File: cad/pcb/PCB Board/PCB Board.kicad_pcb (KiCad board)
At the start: 2 copper layers, 14 parts, among them J1 Conn_01x02_Pin, J2 Conn_01x03_Pin, J3 Conn_01x04_Pin, J4 Conn_01x03_Pin, Q1 BC547, Q2 BC547, Q3 BC547, SW1 SW_Push, SW2 SW_Push, SW3 SW_Push, SW4 SW_Push

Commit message: started work on the pcb and cad data
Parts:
- removed J4: Conn_01x03_Pin, Connector_JST:JST_XH_B3B-XH-A_1x03_P2.50mm_Vertical
- removed Q1, Q2, Q3: BC547, Package_TO_SOT_THT:TO-92_Inline
- removed R1, R2, R3: R33K, Resistor_THT:R_Axial_DIN0204_L3.6mm_D1.6mm_P7.62mm_Horizontal
- added StepUp1: ~, Library:StepUp, B.Cu at (143.2, 64.5)
- added U1: BOB-12009, BOB-12009:CONV_BOB-12009, B.Cu at (142.9, 88.1)
- added U2: ~, Library:Lolin32 Lite, B.Cu at (135.5, 50.4)
- J1: value Conn_01x02_Pin -> POWER; moved to B.Cu
- J2: value Conn_01x03_Pin -> LED+
- J3: value Conn_01x04_Pin -> Conn_01x02_Pin; footprint Connector_JST:JST_XH_B4B-XH-A_1x04_P2.50mm_Vertical -> Connector_Wire:SolderWire-0.1sqmm_1x02_P3.6mm_D0.4mm_OD1mm; moved to B.Cu
- moved SW4 118.7 mm to (93.0, 78.2), turned to 90 degrees
- moved J1 80.2 mm to (101.0, 63.0), turned to 180 degrees
- moved SW3 77.4 mm to (128.0, 107.2), turned to 180 degrees
- moved J2 73.8 mm to (124.2, 75.0), turned to 90 degrees
- moved J3 65.1 mm to (104.0, 70.2)
- moved SW2 62.7 mm to (158.0, 71.5), turned to -90 degrees
- moved SW1 62.5 mm to (122.0, 42.5)
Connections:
- J1 pad 2: Net-(J1-Pin_2) -> GND
- J2 pad 1: Net-(J1-Pin_1) -> Net-(J2-Pin_1)
- J2 pad 2: Net-(J1-Pin_1) -> Net-(J2-Pin_2)
- J2 pad 3: Net-(J1-Pin_1) -> Net-(J2-Pin_3)
- J3 pad 1: Net-(J3-Pin_1) -> Net-(J1-Pin_1)
- J3 pad 2: Net-(J3-Pin_2) -> GND
- SW1 pad 1: Net-(J3-Pin_4) -> Net-(J1-Pin_2)
- SW1 pad 2: Net-(J1-Pin_2) -> Net-(SW1-Pad2)
- SW2 pad 1: Net-(J3-Pin_4) -> GND
- SW2 pad 2: Net-(J1-Pin_2) -> Net-(SW1-Pad2)
- SW3 pad 1: Net-(J3-Pin_4) -> GND
- SW3 pad 2: Net-(J1-Pin_2) -> Net-(SW1-Pad2)
- SW4 pad 1: Net-(J3-Pin_4) -> GND
- SW4 pad 2: Net-(J1-Pin_2) -> Net-(SW1-Pad2)
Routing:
- net GND: track 0.00 -> 200.4 mm
- net Net-(SW1-Pad2): track 0.00 -> 141.0 mm
- net Net-(J1-Pin_1): track 0.00 -> 62.1 mm
- net Net-(U1-PadLV): track 0.00 -> 37.1 mm
- net Net-(J2-Pin_3): track 0.00 -> 31.1 mm
- net Net-(J2-Pin_2): track 0.00 -> 25.5 mm
- net Net-(J2-Pin_1): track 0.00 -> 16.4 mm
- net Net-(U1-PadLV1): track 0.00 -> 16.1 mm
- added copper zone on B.Cu, net GND
- added copper zone on F.Cu, net GND
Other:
- board outline added: 70 x 70 mm

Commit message: continued work on pcb
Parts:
- moved SW2 1.00 mm to (157.0, 71.5)
- moved SW1 0.75 mm to (122.0, 43.2)
- moved SW4 0.75 mm to (93.8, 78.2)
- moved SW3 0.50 mm to (128.0, 106.8)
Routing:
- net Net-(SW1-Pad2): track 141.0 -> 167.0 mm
- net GND: track 200.4 -> 199.4 mm
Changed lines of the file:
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@@
 	(footprint "Button_Switch_THT:SW_PUSH_6mm_H5mm"
 		(layer "F.Cu")
-		(at 122 42.5)
+		(at 122 43.25)
 		(descr "tactile push button, 6x6mm e.g. PHAP33xx series, height=5mm")
 		(tags "tact sw push 6mm")
 		(property "Reference" "SW1"
-			(at 3.25 -2 0)
+			(at 3.25 2.25 0)
 			(layer "F.SilkS")
 			(effects
@@
 	(footprint "Button_Switch_THT:SW_PUSH_6mm_H5mm"
 		(layer "F.Cu")
-		(at 158 71.5 -90)
+		(at 157 71.5 -90)
 		(descr "tactile push button, 6x6mm e.g. PHAP33xx series, height=5mm")
 		(tags "tact sw push 6mm")
 		(property "Reference" "SW2"
-			(at 3 -3.25 90)
+			(at 3.25 2 90)
 			(layer "F.SilkS")
 			(effects
@@
 		)
 		(fp_text user "${REFERENCE}"
-			(at -8.75 1.5 90)
+			(at -3.25 2.25 90)
 			(layer "F.Fab")
 			(effects
@@
 	(footprint "Button_Switch_THT:SW_PUSH_6mm_H5mm"
 		(layer "F.Cu")
-		(at 93 78.25 90)
+		(at 93.75 78.25 90)
 		(descr "tactile push button, 6x6mm e.g. PHAP33xx series, height=5mm")
 		(tags "tact sw push 6mm")
 		(property "Reference" "SW4"
-			(at 3.25 -2 -90)
+			(at -3.25 1.5 -90)
 			(layer "F.SilkS")
 			(effects
@@
 	(footprint "Button_Switch_THT:SW_PUSH_6mm_H5mm"
 		(layer "F.Cu")
-		(at 128 107.25 180)
+		(at 128 106.75 180)
 		(descr "tactile push button, 6x6mm e.g. PHAP33xx series, height=5mm")
 		(tags "tact sw push 6mm")
 		(property "Reference" "SW3"
-			(at 3.25 -2 180)
+			(at -3.75 0.25 180)
 			(layer "F.SilkS")
 			(effects
@@
 		(layer "Edge.Cuts")
 	)
+	(gr_circle
+		(center 125.5 75)
+		(end 159.5 75)
+		(stroke
+			(width 0.1)
+			(type default)
+		)
+		(fill none)
+		(layer "Margin")
+	)
 	(segment
 		(start 124.25 75)
@@
 	)
 	(segment
+		(start 128.5 47.75)
+		(end 122 47.75)
+		(width 0.2)
+		(layer "F.Cu")
+		(net 3)
+	)
+	(segment
+		(start 128 102.25)
+		(end 121.5 102.25)
+		(width 0.2)
+		(layer "F.Cu")
+		(net 3)
+	)
+	(segment
+		(start 152.5 78)
+		(end 152.5 71.5)
+		(width 0.2)
+		(layer "F.Cu")
+		(net 3)
+	)
+	(segment
+		(start 98.25 78.25)
+		(end 98.25 71.75)
+		(width 0.2)
+		(layer "F.Cu")
+		(net 3)
+	)
+	(segment
 		(start 139.257369 57.257369)
 		(end 117.742631 57.257369)
@@
 	)
 	(segment
-		(start 151.25 96.25)
-		(end 148.5 99)
+		(start 151.17 86.83)
+		(end 151.25 86.75)
 		(width 0.2)
 		(layer "F.Cu")
@@
 	)
 	(segment
-		(start 134.25 98.5)
-		(end 134.25 92.53)
+		(start 148 86.83)
+		(end 151.17 86.83)
 		(width 0.2)
 		(layer "F.Cu")
@@
 	)
 	(segment
-		(start 151.17 86.83)
-		(end 151.25 86.75)
+		(start 151.25 86.75)
+		(end 151.25 95.5)
 		(width 0.2)
 		(layer "F.Cu")
@@
 	)
 	(segment
-		(start 148 86.83)
-		(end 151.17 86.83)
+		(start 151.25 95.5)
+		(end 147.75 99)
 		(width 0.2)
 		(layer "F.Cu")
@@
 	)
 	(segment
-		(start 151.25 86.75)
-		(end 151.25 96.25)
+		(start 134.75 99)
+		(end 134.25 98.5)
 		(width 0.2)
 		(layer "F.Cu")
@@
 	)
 	(segment
-		(start 134.75 99)
-		(end 134.25 98.5)
+		(start 147.75 99)
+		(end 134.75 99)
 		(width 0.2)
 		(layer "F.Cu")
@@
 	)
 	(segment
-		(start 148.5 99)
-		(end 134.75 99)
+		(start 134.25 98.5)
+		(end 134.25 92.53)
 		(width 0.2)
 		(layer "F.Cu")
@@
 	)
 	(segment
-		(start 118 106.5)
-		(end 118.75 107.25)
+		(start 106.39 63.36)
+		(end 101.25 68.5)
 		(width 0.2)
 		(layer "B.Cu")
@@
 	)
 	(segment
-		(start 106.39 63.36)
-		(end 101.25 68.5)
+		(start 143.25 92)
+		(end 128 107.25)
 		(width 0.2)
 		(layer "B.Cu")
@@
 	)
 	(segment
-		(start 93 78.25)
-		(end 93 81.53886)
+		(start 158 78)
+		(end 158 71.5)
 		(width 0.2)
 		(layer "B.Cu")
@@
 	)
 	(segment
-		(start 143.25 92)
-		(end 128 107.25)
+		(start 93 71.75)
+		(end 93 81.53886)
 		(width 0.2)
 		(layer "B.Cu")
@@
 	)
 	(segment
-		(start 158 78)
-		(end 158 71.5)
+		(start 98.25 69.25)
+		(end 95.5 69.25)
 		(width 0.2)
 		(layer "B.Cu")
@@
 	)
 	(segment
-		(start 98.5 70.45)
-		(end 94.3 70.45)
+		(start 101.25 68.5)
+		(end 100.25 69.5)
 		(width 0.2)
 		(layer "B.Cu")
@@
 	)
 	(segment
-		(start 94.3 70.45)
-		(end 93 71.75)
+		(start 104 73.75)
+		(end 104 73.25)
 		(width 0.2)
 		(layer "B.Cu")
@@
 	)
 	(segment
-		(start 158 79.37)
-		(end 148 89.37)
+		(start 118 106.5)
+		(end 118.75 107.25)
 		(width 0.2)
 		(layer "B.Cu")
@@
 	)
 	(segment
-		(start 99.25 70.45)
-		(end 98.5 70.45)
+		(start 158 79.37)
+		(end 148 89.37)
 		(width 0.2)
 		(layer "B.Cu")
@@
 	)
 	(segment
-		(start 118.75 107.25)
-		(end 121.5 107.25)
+		(start 98.5 69.25)
+		(end 98.5 63)
 		(width 0.2)
 		(layer "B.Cu")
@@
 	)
 	(segment
-		(start 104 73.75)
-		(end 102.55 73.75)
+		(start 118.75 107.25)
+		(end 128 107.25)
 		(width 0.2)
 		(layer "B.Cu")
@@
 	)
 	(segment
-		(start 93 81.53886)
-		(end 117.96114 106.5)
+		(start 143.25 89.37)
+		(end 143.25 92)
 		(width 0.2)
 		(layer "B.Cu")
@@
 	)
 	(segment
-		(start 102.55 73.75)
-		(end 99.25 70.45)
+		(start 143.25 55)
+		(end 158 69.75)
 		(width 0.2)
 		(layer "B.Cu")
@@
 	)
 	(segment
-		(start 117.96114 106.5)
-		(end 118 106.5)
+		(start 95.5 69.25)
+		(end 93 71.75)
 		(width 0.2)
 		(layer "B.Cu")
@@
 	)
 	(segment
-		(start 143.25 89.37)
-		(end 143.25 92)
+		(start 100.25 69.5)
+		(end 98.5 69.5)
 		(width 0.2)
 		(layer "B.Cu")
@@
 	)
 	(segment
-		(start 143.25 55)
-		(end 158 69.75)
+		(start 106.39 62)
+		(end 106.39 63.36)
 		(width 0.2)
 		(layer "B.Cu")
@@
 	)
 	(segment
-		(start 106.39 62)
-		(end 106.39 63.36)
+		(start 93 81.53886)
+		(end 117.96114 106.5)
 		(width 0.2)
 		(layer "B.Cu")
@@
 	)
 	(segment
-		(start 93 71.75)
-		(end 93 78.25)
+		(start 117.96114 106.5)
+		(end 118 106.5)
 		(width 0.2)
 		(layer "B.Cu")
@@
 	)
 	(segment
-		(start 128 107.25)
-		(end 121.5 107.25)
+		(start 104 73.25)
+		(end 100.25 69.5)
 		(width 0.2)
 		(layer "B.Cu")
@@
 	)
 	(segment
-		(start 98.5 63)
-		(end 98.5 70.45)
+		(start 98.5 69.25)
+		(end 98.25 69.25)
 		(width 0.2)
 		(layer "B.Cu")
@@
 	)
 	(segment
-		(start 128 107.25)
-		(end 129.75 105.5)
+		(start 98.5 69.5)
+		(end 98.25 69.25)
 		(width 0.2)
 		(layer "B.Cu")
@@
 	)
 	(segment
-		(start 99.3 70.45)
-		(end 99.25 70.45)
+		(start 128 107.25)
+		(end 129.75 105.5)
 		(width 0.2)
 		(layer "B.Cu")
@@
 	)
 	(segment
-		(start 101.25 68.5)
-		(end 99.3 70.45)
+		(start 99.3 70.45)
+		(end 99.25 70.45)
 		(width 0.2)
 		(layer "B.Cu")

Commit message: updated pcbs
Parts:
- added J4: ON_OFF_SWITCH, Connector_Wire:SolderWire-0.5sqmm_1x02_P4.6mm_D0.9mm_OD2.1mm_Relief, B.Cu at (81.2, 48.8)
- added REF**: MountingHole_3.2mm_M3_Pad, MountingHole:MountingHole_3.2mm_M3_Pad, F.Cu at (101.8, 63.9)
- added REF**: MountingHole_3.2mm_M3_Pad, MountingHole:MountingHole_3.2mm_M3_Pad, F.Cu at (64.6, 101.1)
- added REF**: MountingHole_5.3mm_M5_DIN965, MountingHole:MountingHole_5.3mm_M5_DIN965, F.Cu at (80.5, 94.0)
- added REF**: MountingHole_3.2mm_M3_Pad, MountingHole:MountingHole_3.2mm_M3_Pad, F.Cu at (27.4, 63.9)
- added REF**: MountingHole_3.2mm_M3_Pad, MountingHole:MountingHole_3.2mm_M3_Pad, F.Cu at (64.6, 26.7)
- J1, StepUp1, U2: moved to F.Cu
- J3: value Conn_01x02_Pin -> BATTERY_CONNECTOR; footprint Connector_Wire:SolderWire-0.1sqmm_1x02_P3.6mm_D0.4mm_OD1mm -> Connector_Wire:SolderWire-0.5sqmm_1x02_P4.6mm_D0.9mm_OD2.1mm_Relief; moved to F.Cu
- SW1, SW2, SW3, SW4: moved to B.Cu
- U1: value BOB-12009 -> Lvl-Shifter; moved to F.Cu
- moved SW2 124.4 mm to (33.1, 60.4)
- moved U2 106.5 mm to (29.1, 46.8), turned to 45 degrees
- moved StepUp1 96.8 mm to (47.5, 78.6), turned to -45 degrees
- moved SW3 67.4 mm to (61.6, 95.4), turned to 0 degrees
- moved U1 62.2 mm to (82.0, 75.3), turned to -45 degrees
- moved SW1 55.5 mm to (67.6, 32.4), turned to 180 degrees
- moved J2 54.5 mm to (70.4, 82.9), turned to -45 degrees
- moved J3 34.6 mm to (76.7, 48.8), turned to 180 degrees
- moved J1 20.2 mm to (82.4, 55.2), turned to 0 degrees
- moved SW4 11.6 mm to (96.1, 66.9)
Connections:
- J1 pad 2: GND -> Net-(J1-Pin_2)
- J3 pad 1: Net-(J1-Pin_1) -> Net-(J3-Pin_1)
- J3 pad 2: GND -> Net-(J1-Pin_2)
- SW2 pad 1: GND -> Net-(J1-Pin_2)
- SW3 pad 1: GND -> Net-(J1-Pin_2)
- SW4 pad 1: GND -> Net-(J1-Pin_2)
- StepUp1 pad 1: GND -> Net-(J1-Pin_2)
- StepUp1 pad 2: Net-(J1-Pin_1) -> Net-(J3-Pin_1)
- U1 pad GND_1: GND -> Net-(J1-Pin_2)
- U1 pad GND_2: GND -> Net-(J1-Pin_2)
- U2 pad GND: GND -> Net-(J1-Pin_2)
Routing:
- net Net-(J1-Pin_2): track 0.00 -> 257.2 mm
- net GND: track 199.4 -> 0.00 mm
- net Net-(J3-Pin_1): track 0.00 -> 67.7 mm, vias 0 -> 2
- net Net-(J1-Pin_1): track 62.1 -> 7.78 mm
- net Net-(U1-PadLV): track 36.7 -> 21.5 mm
- net Net-(U1-PadLV1): track 16.1 -> 28.7 mm
- net Net-(SW1-Pad2): track 167.0 -> 155.8 mm
- net Net-(J2-Pin_3): track 31.1 -> 38.7 mm
- net Net-(J2-Pin_1): track 16.4 -> 23.2 mm
- net Net-(J2-Pin_2): track 25.5 -> 22.4 mm
- added copper zone on B.Cu, net Net-(J1-Pin_2)
- added copper zone on F.Cu, net Net-(J1-Pin_2)
- removed copper zone on B.Cu, net GND
- removed copper zone on F.Cu, net GND
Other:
- board size 70 x 70 mm -> 84 x 84 mm

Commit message: [WIP] save changes
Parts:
- removed J3: BATTERY_CONNECTOR, Connector_Wire:SolderWire-0.5sqmm_1x02_P4.6mm_D0.9mm_OD2.1mm_Relief
- removed J4: ON_OFF_SWITCH, Connector_Wire:SolderWire-0.5sqmm_1x02_P4.6mm_D0.9mm_OD2.1mm_Relief
- removed REF** (x4): MountingHole_3.2mm_M3_Pad, MountingHole:MountingHole_3.2mm_M3_Pad
- removed REF**: MountingHole_5.3mm_M5_DIN965, MountingHole:MountingHole_5.3mm_M5_DIN965
- removed StepUp1: ~, Library:StepUp
- added C1: C1uF, Capacitor_SMD:C_0402_1005Metric, F.Cu at (37.1, 37.9)
- added C10: C1uF, Capacitor_SMD:C_0402_1005Metric, F.Cu at (46.6, 85.3)
- added C11: C1uF, Capacitor_SMD:C_0402_1005Metric, F.Cu at (37.0, 68.8)
- added C13: C1uF, Capacitor_SMD:C_0402_1005Metric, F.Cu at (64.6, 35.4)
- added C14: C1uF, Capacitor_SMD:C_0402_1005Metric, F.Cu at (92.2, 59.0)
- added C15: C1uF, Capacitor_SMD:C_0402_1005Metric, F.Cu at (46.6, 42.5)
- added C16: C1uF, Capacitor_SMD:C_0402_1005Metric, F.Cu at (37.0, 59.0)
- added C17: C1uF, Capacitor_SMD:C_0402_1005Metric, F.Cu at (82.6, 42.5)
- added C2: C10uF, Capacitor_SMD:C_0402_1005Metric, F.Cu at (54.1, 76.4)
- added C3: C1uF, Capacitor_SMD:C_0402_1005Metric, F.Cu at (61.6, 75.9)
- added C4: C2.2uF, Capacitor_SMD:C_0402_1005Metric, F.Cu at (77.1, 78.9)
- added C5: C10uF, Capacitor_SMD:C_0402_1005Metric, F.Cu at (78.1, 73.4)
- added C7: C1uF, Capacitor_SMD:C_0402_1005Metric, F.Cu at (92.2, 68.8)
- added C8: C1uF, Capacitor_SMD:C_0402_1005Metric, F.Cu at (82.6, 85.3)
- added C9: C1uF, Capacitor_SMD:C_0402_1005Metric, F.Cu at (64.6, 91.9)
- added D1: SS14, Diode_SMD:D_SMA, F.Cu at (65.6, 79.9)
- added D10: SK6812, LED_SMD:LED_SK6812_PLCC4_5.0x5.0mm_P3.2mm, F.Cu at (78.6, 88.1)
- added D11: SK6812, LED_SMD:LED_SK6812_PLCC4_5.0x5.0mm_P3.2mm, F.Cu at (86.0, 81.9)
- added D12: SK6812, LED_SMD:LED_SK6812_PLCC4_5.0x5.0mm_P3.2mm, F.Cu at (90.9, 73.5)
- added D13: SK6812, LED_SMD:LED_SK6812_PLCC4_5.0x5.0mm_P3.2mm, F.Cu at (92.6, 63.9)
- added D14: SK6812, LED_SMD:LED_SK6812_PLCC4_5.0x5.0mm_P3.2mm, F.Cu at (90.9, 54.3)
- added D15: SK6812, LED_SMD:LED_SK6812_PLCC4_5.0x5.0mm_P3.2mm, F.Cu at (86.0, 45.9)
- added D16: SK6812, LED_SMD:LED_SK6812_PLCC4_5.0x5.0mm_P3.2mm, F.Cu at (78.6, 39.7)
- added D17: SK6812, LED_SMD:LED_SK6812_PLCC4_5.0x5.0mm_P3.2mm, F.Cu at (69.5, 36.3)
- added D18: SK6812, LED_SMD:LED_SK6812_PLCC4_5.0x5.0mm_P3.2mm, F.Cu at (59.7, 36.3)
- added D19: SK6812, LED_SMD:LED_SK6812_PLCC4_5.0x5.0mm_P3.2mm, F.Cu at (50.6, 39.7)
- added D2: 150040VS73220, LED_SMD:LED_0402_1005Metric, F.Cu at (98.6, 39.9)
- added D20: SK6812, LED_SMD:LED_SK6812_PLCC4_5.0x5.0mm_P3.2mm, F.Cu at (43.2, 45.9)
- added D21: SK6812, LED_SMD:LED_SK6812_PLCC4_5.0x5.0mm_P3.2mm, F.Cu at (38.3, 54.3)
- added D3: 150040BS73220, LED_SMD:LED_0402_1005Metric, F.Cu at (86.6, 30.4)
- added D4: SK6812, LED_SMD:LED_SK6812_PLCC4_5.0x5.0mm_P3.2mm, F.Cu at (36.6, 63.9)
- added D5: SK6812, LED_SMD:LED_SK6812_PLCC4_5.0x5.0mm_P3.2mm, F.Cu at (38.3, 73.5)
- added D6: SK6812, LED_SMD:LED_SK6812_PLCC4_5.0x5.0mm_P3.2mm, F.Cu at (43.2, 81.9)
- added D7: SK6812, LED_SMD:LED_SK6812_PLCC4_5.0x5.0mm_P3.2mm, F.Cu at (50.6, 88.1)
- added D8: SK6812, LED_SMD:LED_SK6812_PLCC4_5.0x5.0mm_P3.2mm, F.Cu at (59.7, 91.5)
- added D9: SK6812, LED_SMD:LED_SK6812_PLCC4_5.0x5.0mm_P3.2mm, F.Cu at (69.5, 91.5)
- added H2: MountingHole_Pad, MountingHole:MountingHole_3.2mm_M3_DIN965_Pad_TopBottom, F.Cu at (82.1, 96.9)
- added H3: MountingHole_Pad, MountingHole:MountingHole_3.2mm_M3_DIN965_Pad_TopBottom, F.Cu at (53.6, 27.9)
- added H4: MountingHole_Pad, MountingHole:MountingHole_3.2mm_M3_DIN965_Pad_TopBottom, F.Cu at (31.1, 79.9)
- added Q1: FDN340P, Package_TO_SOT_SMD:SOT-23, F.Cu at (72.0, 81.0)
- added Q2: BSS138, Package_TO_SOT_SMD:SOT-23, F.Cu at (44.2, 68.4)
- added R1: R10K, Resistor_SMD:R_0402_1005Metric, F.Cu at (51.6, 58.9)
- added R10: R10K, Resistor_SMD:R_0402_1005Metric, F.Cu at (79.1, 61.9)
- added R11: R330, Resistor_SMD:R_0402_1005Metric, F.Cu at (99.1, 45.4)
- added R12: R10K, Resistor_SMD:R_0402_1005Metric, F.Cu at (51.6, 65.4)
- added R13: R10K, Resistor_SMD:R_0402_1005Metric, F.Cu at (47.1, 68.9)
- added R14: R470, Resistor_SMD:R_0402_1005Metric, F.Cu at (43.6, 60.4)
- added R15: R2K, Resistor_SMD:R_0402_1005Metric, F.Cu at (80.6, 78.9)
- added R2: R5.1k, Resistor_SMD:R_0402_1005Metric, F.Cu at (84.6, 34.9)
- added R3: R5.1k, Resistor_SMD:R_0402_1005Metric, F.Cu at (95.2, 42.3)
- added R4: R10K, Resistor_SMD:R_0402_1005Metric, F.Cu at (76.6, 60.9)
- added R5: R10K, Resistor_SMD:R_0402_1005Metric, F.Cu at (51.6, 66.9)
- added R6: R100K, Resistor_SMD:R_0402_1005Metric, F.Cu at (51.1, 61.4)
- added R7: R100K, Resistor_SMD:R_0402_1005Metric, F.Cu at (49.6, 61.4)
- added R8: R100K, Resistor_SMD:R_0402_1005Metric, F.Cu at (71.1, 75.9)
- added R9: R100K, Resistor_SMD:R_0402_1005Metric, F.Cu at (51.1, 76.4)
- added SW5: PTS645, Button_Switch_SMD:SW_SPST_PTS645, F.Cu at (64.6, 26.9)
- added SW6: PTS645, Button_Switch_SMD:SW_SPST_PTS645, F.Cu at (27.6, 63.9)
- added SW7: SLW-1277545-3A-RA-N-D, Button_Switch_THT:SW_Slide_SPDT_Angled_CK_OS102011MA1Q, F.Cu at (91.5, 90.8)
- added U3: TP4057, Package_TO_SOT_SMD:TSOT-23-6, F.Cu at (78.7, 76.3)
- J1: value POWER -> USB4105; footprint Connector_JST:JST_XH_B2B-XH-A_1x02_P2.50mm_Vertical -> Connector_USB:USB_C_Receptacle_GCT_USB4105-xx-A_16P_TopMnt_Horizontal
- J2: value LED+ -> S2B-PH-K-S; footprint Connector_JST:JST_XH_B3B-XH-A_1x03_P2.50mm_Vertical -> Connector_JST:JST_PH_S2B-PH-K_1x02_P2.00mm_Horizontal
- SW1, SW2, SW3, SW4: value SW_Push -> PTS645; footprint Button_Switch_THT:SW_PUSH_6mm_H5mm -> Button_Switch_SMD:SW_SPST_PTS645; moved to F.Cu
- U1: value Lvl-Shifter -> ESP32-C3-WROOM-02; footprint BOB-12009:CONV_BOB-12009 -> RF_Module:ESP32-C3-WROOM-02
- U2: value ~ -> TLV75533PDYDR; footprint Library:Lolin32 Lite -> Package_TO_SOT_SMD:SOT-23-5
- moved U2 41.4 mm to (57.6, 76.9), turned to 0 degrees
- moved J2 26.2 mm to (96.5, 81.8), turned to 135 degrees
- moved SW1 24.0 mm to (43.6, 33.7), turned to -140 degrees
- moved J1 21.4 mm to (92.6, 36.4), turned to 135 degrees
- moved U1 20.8 mm to (64.6, 63.9), turned to 0 degrees
- moved SW2 14.4 mm to (32.4, 46.1), turned to 65 degrees
- moved SW4 6.26 mm to (101.6, 63.9), turned to -90 degrees
- moved SW3 6.26 mm to (64.6, 100.9), turned to 180 degrees
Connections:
- J2 pad 2: Net-(J2-Pin_2) -> VBAT
- SW1 pad 1: Net-(J1-Pin_2) -> EN
- SW1 pad 2: Net-(SW1-Pad2) -> GND
- SW2 pad 1: Net-(J1-Pin_2) -> GND
- SW2 pad 2: Net-(SW1-Pad2) -> IO9
- SW3 pad 1: Net-(J1-Pin_2) -> GND
- SW3 pad 2: Net-(SW1-Pad2) -> IO3
- SW4 pad 1: Net-(J1-Pin_2) -> GND
- SW4 pad 2: Net-(SW1-Pad2) -> IO3
- U2 pad 2: unconnected-(U2-Pad2) -> GND
- U2 pad 5: unconnected-(U2-Pad5) -> 3V3
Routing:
- net VIN: track 0.00 -> 297.9 mm
- net Net-(J1-Pin_2): track 257.2 -> 0.00 mm
- net IO3: track 0.00 -> 211.2 mm, vias 0 -> 4
- net Net-(SW1-Pad2): track 155.8 -> 0.00 mm
- net VBUS: track 0.00 -> 133.0 mm, vias 0 -> 6
- net 3V3: track 0.00 -> 78.1 mm, vias 0 -> 4
- net Net-(D3-K): track 0.00 -> 68.5 mm, vias 0 -> 4
- net Net-(J3-Pin_1): track 67.7 -> 0.00 mm, vias 2 -> 0
- net VBAT: track 0.00 -> 64.6 mm, vias 0 -> 3
- net IO9: track 0.00 -> 54.9 mm, vias 0 -> 2
- net EN: track 0.00 -> 49.1 mm, vias 0 -> 2
- net D-: track 0.00 -> 46.5 mm, vias 0 -> 5
- net Net-(D2-K): track 0.00 -> 46.3 mm, vias 0 -> 2
- net D+: track 0.00 -> 45.3 mm, vias 0 -> 4
- net GND: track 0.00 -> 40.6 mm, vias 0 -> 16
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- added copper zone on B.Cu, net GND
- added copper zone on F.Cu, net GND
- removed copper zone on B.Cu, net Net-(J1-Pin_2)
- removed copper zone on F.Cu, net Net-(J1-Pin_2)
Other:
- board size 84 x 84 mm -> 86 x 86 mm
- board text added: "BOOT"
- board text added: "RST"

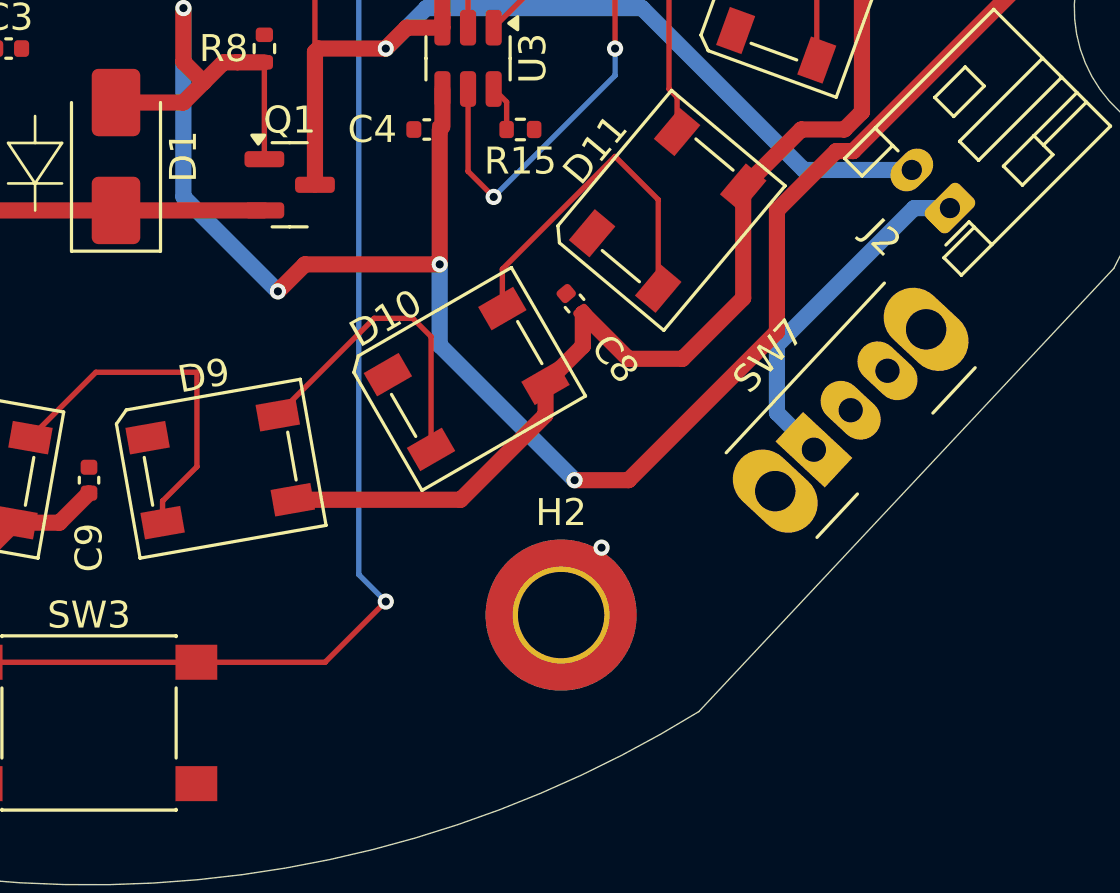
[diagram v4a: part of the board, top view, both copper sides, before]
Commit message: updated with charging circuit
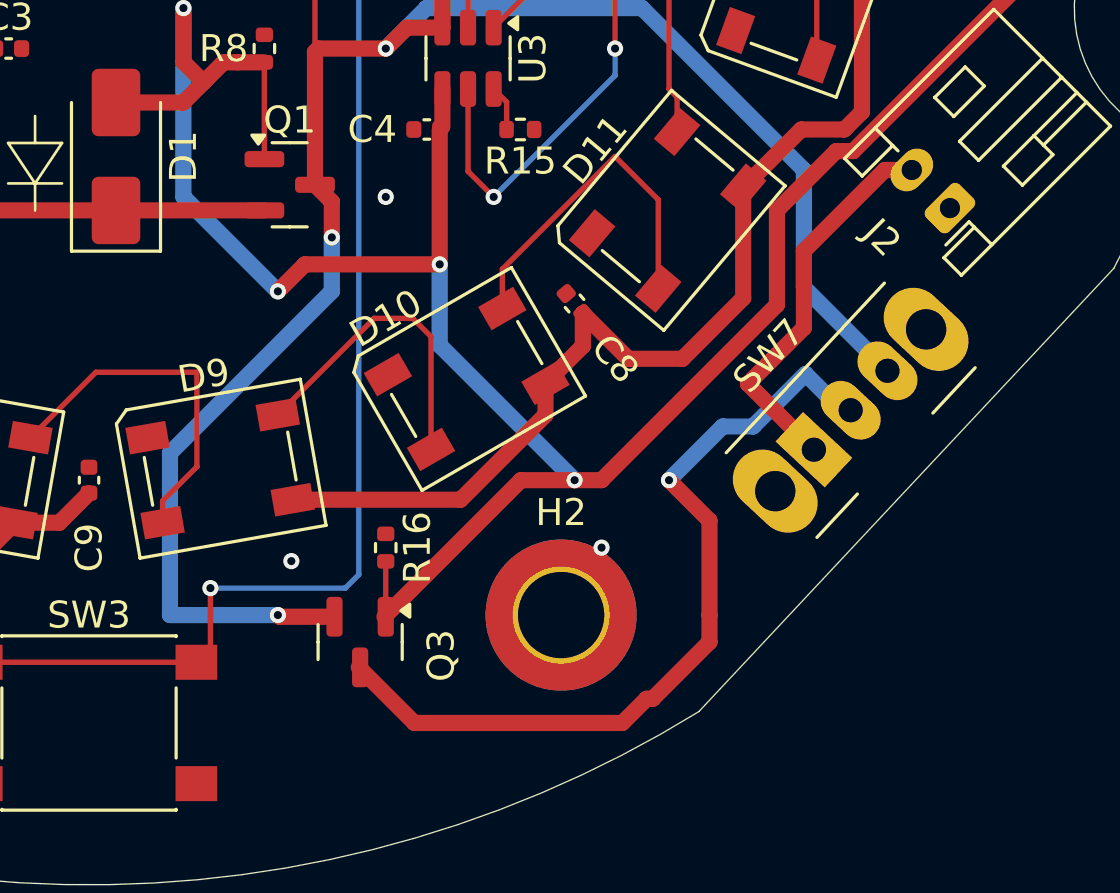
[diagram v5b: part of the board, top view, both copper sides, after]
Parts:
- added Q3: MMFTN170, Package_TO_SOT_SMD:SOT-23, F.Cu at (74.7, 97.9)
- added R16: R10K, Resistor_SMD:R_0402_1005Metric, F.Cu at (75.6, 94.4)
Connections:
- J2 pad 1: Net-(J2-Pin_1) -> GND
- J2 pad 2: VBAT -> Net-(J2-Pin_2)
- SW7 pad 1: Net-(J2-Pin_1) -> Net-(J2-Pin_2)
- SW7 pad 2: unconnected-(SW7-C-Pad2) -> Net-(Q3-D)
- SW7 pad 3: GND -> VBAT
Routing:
- net Net-(Q3-D): track 0.00 -> 31.4 mm, vias 0 -> 1
- net VBAT: track 64.6 -> 94.5 mm, vias 3 -> 5
- net Net-(J2-Pin_2): track 0.00 -> 14.5 mm
- net Net-(J2-Pin_1): track 13.0 -> 0.00 mm
- net VBUS: track 133.0 -> 143.8 mm
- net IO3: track 211.2 -> 210.5 mm
- net GND: track 40.6 -> 40.1 mm, vias 16 -> 18
